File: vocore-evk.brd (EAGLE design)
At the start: 50 x 70 mm, 20 parts, among them CN1 host, CN2 micro, CN3 CON-RJ45-HR911105A, CN4 CON-RJ45-HR911105A, J1 M023.5MM, J2 EJTAG_MIPS, J3 M12X2

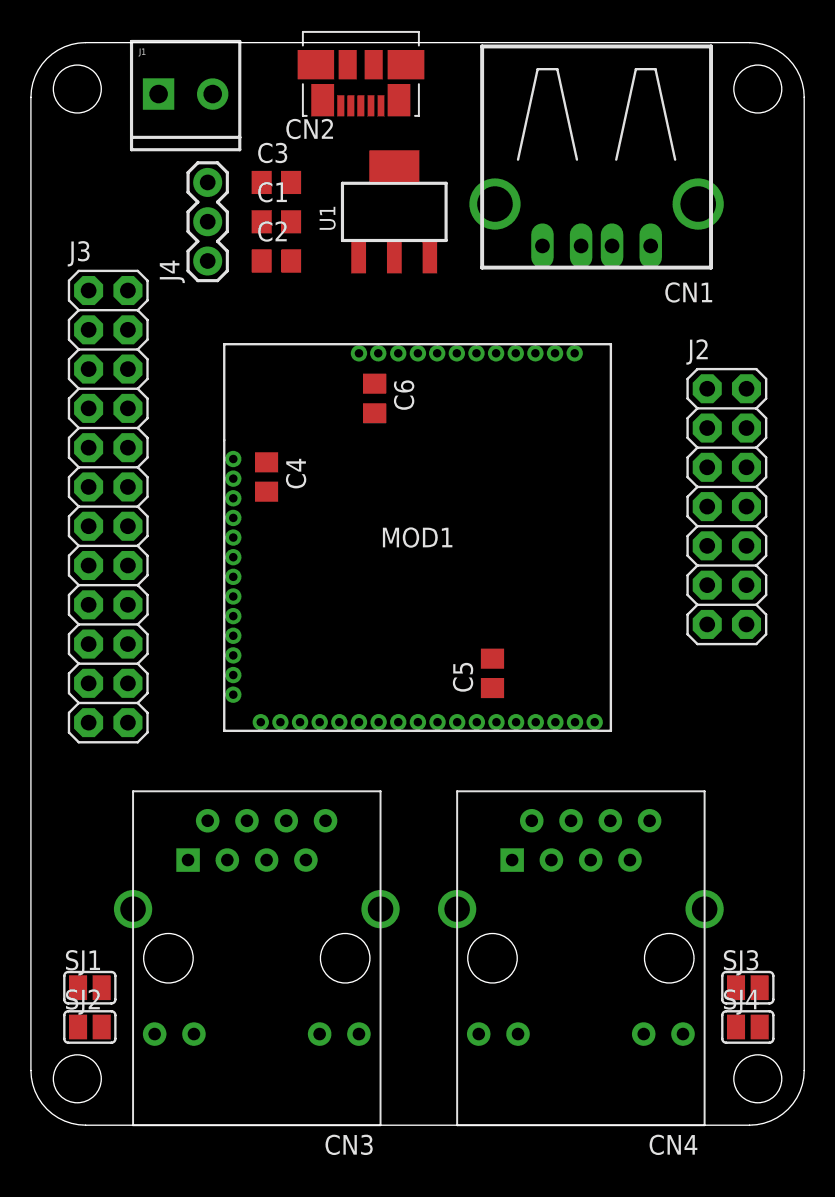
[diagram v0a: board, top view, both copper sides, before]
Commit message: add vocore-evk inital wireing
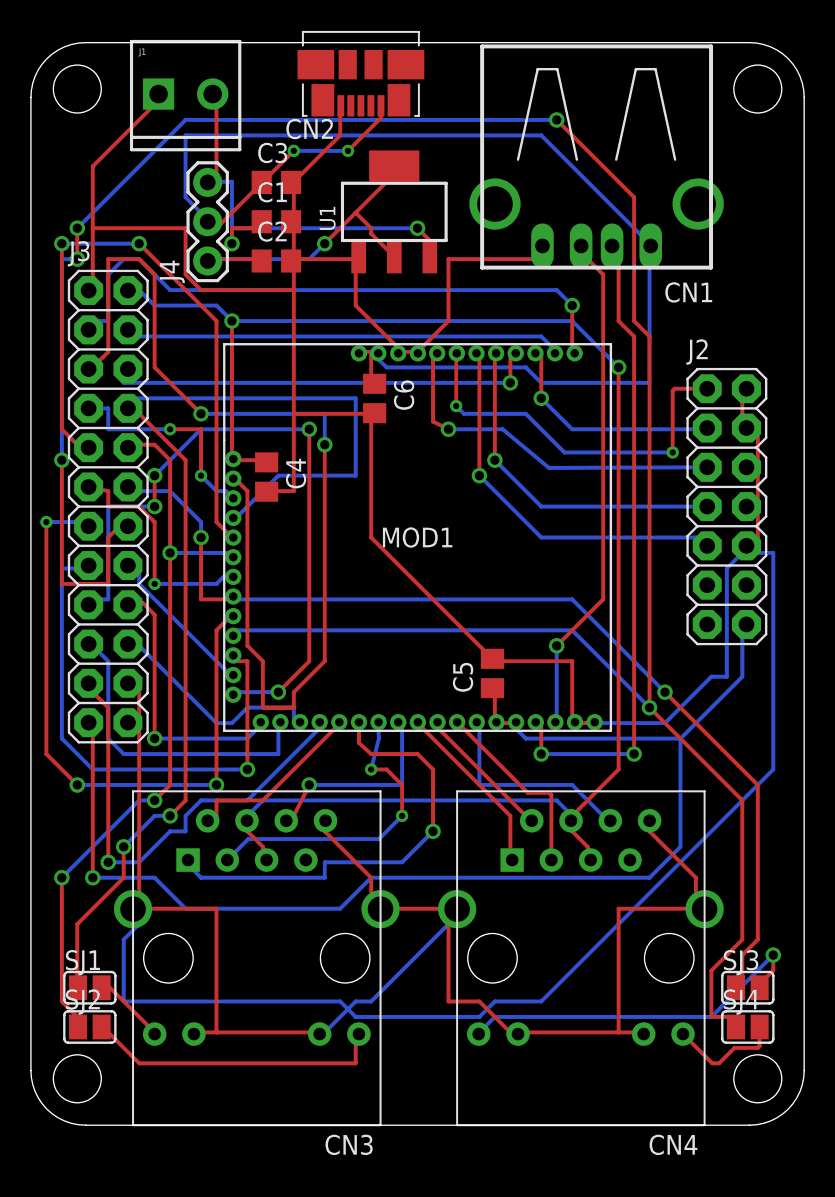
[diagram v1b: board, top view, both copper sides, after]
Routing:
- net GND: track 0.00 -> 328.0 mm
- net GP25: track 0.00 -> 161.5 mm, vias 0 -> 5
- net 1V8: track 0.00 -> 105.0 mm, vias 0 -> 2
- net 5V0: track 0.00 -> 86.4 mm, vias 0 -> 2
- net 3V3: track 0.00 -> 82.5 mm, vias 0 -> 1
- net GP22: track 0.00 -> 72.9 mm, vias 0 -> 2
- net GP12: track 0.00 -> 67.2 mm, vias 0 -> 2
- net GP24: track 0.00 -> 66.9 mm, vias 0 -> 2
- net GP23: track 0.00 -> 48.0 mm, vias 0 -> 3
- net TXD2: track 0.00 -> 44.7 mm, vias 0 -> 4
- net USB_N: track 0.00 -> 41.7 mm, vias 0 -> 2
- net GP27: track 0.00 -> 41.1 mm, vias 0 -> 3
- net GP08: track 0.00 -> 40.7 mm, vias 0 -> 2
- net GP02: track 0.00 -> 39.5 mm, vias 0 -> 1
- net GP14: track 0.00 -> 34.0 mm, vias 0 -> 1
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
